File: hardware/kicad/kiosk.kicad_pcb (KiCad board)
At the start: 2 copper layers, 170 x 116 mm, 15 parts, among them J10 TerminalBlock_MaiXu_MX126-5.0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, J11 TerminalBlock_MaiXu_MX126-5.0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, J13 PinHeader_1x09_P2.54mm_Vertic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, J3 PinSocket_1x14_P2.54mm_Vertic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, J4 PinSocket_1x06_P2.54mm_Vertic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, J5 PinSocket_1x04_P2.54mm_Vertic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, J6 PinSocket_1x06_P2.54mm_Vertic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, J7 PinSocket_1x07_P2.54mm_Vertic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, J9 PinHeader_1x03_P2.54mm_Vertic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, U1 ESP32-S3-CAM

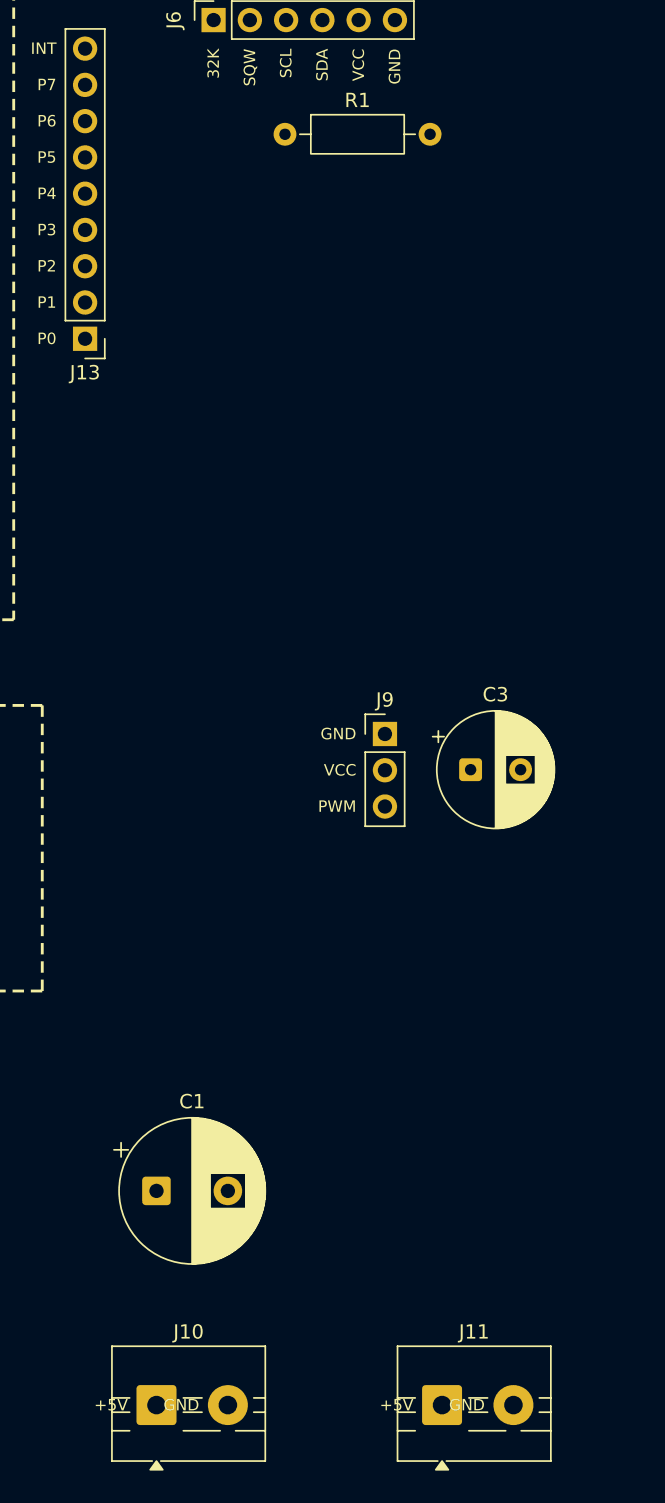
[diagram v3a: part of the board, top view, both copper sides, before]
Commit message: fix(hardware): keep the terminal labels off the neighbouring screw
Both 5 V inputs are two-pad screw terminals at 5.00 mm pitch, and the
label for each pad was set 2 mm inboard of it. On a two-pad row that puts
the text between the pads: "GND" landed on the copper of the +5V screw on
J10 and J11 both. Read off the finished board, either supply would have
gone in backwards. Labels on a two-pad row now grow outward past their own
end, where nothing else can claim them.

R1 is turned round. Its two legs want J6.VCC and J6.SDA, which are the
only pads on the board carrying 3V3 and SDA 2.54 mm apart; drawn the other
way the 3V3 leg reached 9.5 mm and the SDA leg 11.0 mm, against 9.4 and
8.4 now.

Every footprint child arrived without a uuid and pcb upgrade minted a
random one for each, so regenerating the board rewrote about 2000 lines
and buried the real change. They are named from the reference and the node
now, and two runs of the generator produce identical files. This commit
still carries the one-time rewrite.

Task: E14-T8
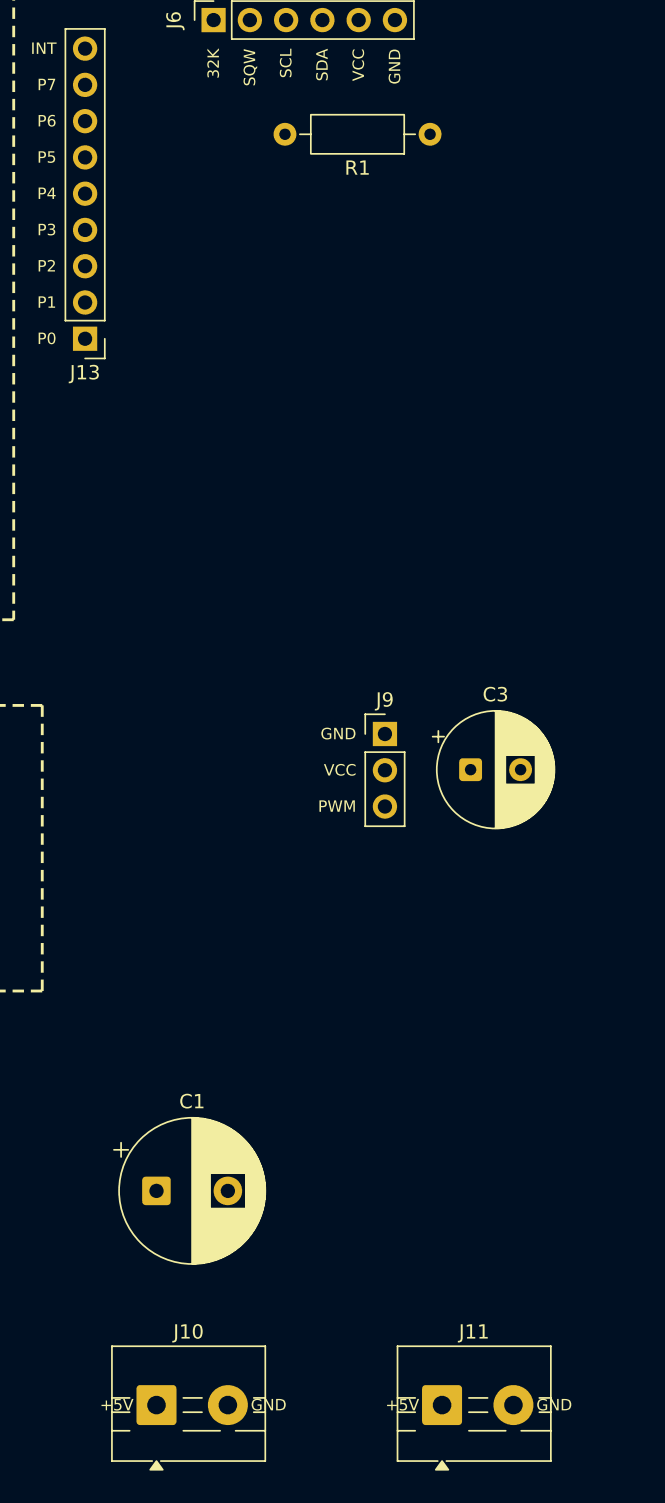
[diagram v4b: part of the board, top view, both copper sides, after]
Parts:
- moved R1 10.2 mm to (153.2, 20.0), turned to 180 degrees
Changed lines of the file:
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@@
 	(footprint "Resistor_THT:R_Axial_DIN0207_L6.3mm_D2.5mm_P10.16mm_Horizontal"
 		(layer "F.Cu")
-		(at 143 20)
+		(at 153.16 20 180)
 		(descr "Resistor, Axial_DIN0207 series, Axial, Horizontal, pin pitch=10.16mm, 0.25W = 1/4W, length*diameter=6.3*2.5mm^2, http://cdn-reichelt.de/documents/datenblatt/B400/1_4W%23YAG.pdf")
 		(tags "Resistor Axial_DIN0207 series Axial Horizontal pin pitch 10.16mm 0.25W = 1/4W length 6.3mm diameter 2.5mm")
 		(property "Reference" "R1"
-			(at 5.08 -2.37 0)
+			(at 5.08 -2.37 180)
 			(layer "F.SilkS")
 			(effects
@@
 		)
 		(property "Value" "R_Axial_DIN0207_L6.3mm_D2.5mm_P10.16mm_Horizontal"
-			(at 5.08 2.37 0)
+			(at 5.08 2.37 180)
 			(layer "F.Fab")
 			(effects
@@
 		)
 		(property "Datasheet" ""
-			(at 0 0 0)
+			(at 0 0 180)
 			(layer "F.Fab")
 			(hide yes)
@@
 		)
 		(property "Description" ""
-			(at 0 0 0)
+			(at 0 0 180)
 			(layer "F.Fab")
 			(hide yes)
@@
 		)
 		(property "KiLib_Generator" "resistor/THT"
-			(at 0 0 0)
+			(at 0 0 180)
 			(layer "F.SilkS")
 			(hide yes)
@@
 		(duplicate_pad_numbers_are_jumpers no)
 		(fp_line
-			(start 1.04 0)
-			(end 1.81 0)
+			(start 9.12 0)
+			(end 8.35 0)
 			(stroke
 				(width 0.12)
@@
 		)
 		(fp_line
-			(start 9.12 0)
-			(end 8.35 0)
+			(start 1.04 0)
+			(end 1.81 0)
 			(stroke
 				(width 0.12)
@@
 		)
 		(fp_line
-			(start 0 0)
-			(end 1.93 0)
+			(start 10.16 0)
+			(end 8.23 0)
 			(stroke
 				(width 0.1)
@@
 		)
 		(fp_line
-			(start 10.16 0)
-			(end 8.23 0)
+			(start 0 0)
+			(end 1.93 0)
 			(stroke
 				(width 0.1)
@@
 		)
 	)
+	(gr_text "GND"
+		(at 140.6 109 0)
+		(layer "F.SilkS")
+		(effects
+			(font
+				(size 0.8 0.8)
+				(thickness 0.12)
+			)
+			(justify left)
+		)
+	)
+	(gr_text "GND"
+		(at 160.6 109 0)
+		(layer "F.SilkS")
+		(effects
+			(font
+				(size 0.8 0.8)
+				(thickness 0.12)
+			)
+			(justify left)
+		)
+	)
 	(gr_text "IO43"
 		(at 28.7 37.87 0)
@@
 	)
 	(gr_text "+5V"
-		(at 132 109 0)
-		(layer "F.SilkS")
-		(effects
-			(font
-				(size 0.8 0.8)
-				(thickness 0.12)
-			)
-			(justify right)
-		)
-	)
-	(gr_text "GND"
-		(at 137 109 0)
+		(at 132.4 109 0)
 		(layer "F.SilkS")
 		(effects
@@
 	)
 	(gr_text "+5V"
-		(at 152 109 0)
-		(layer "F.SilkS")
-		(effects
-			(font
-				(size 0.8 0.8)
-				(thickness 0.12)
-			)
-			(justify right)
-		)
-	)
-	(gr_text "GND"
-		(at 157 109 0)
+		(at 152.4 109 0)
 		(layer "F.SilkS")
 		(effects

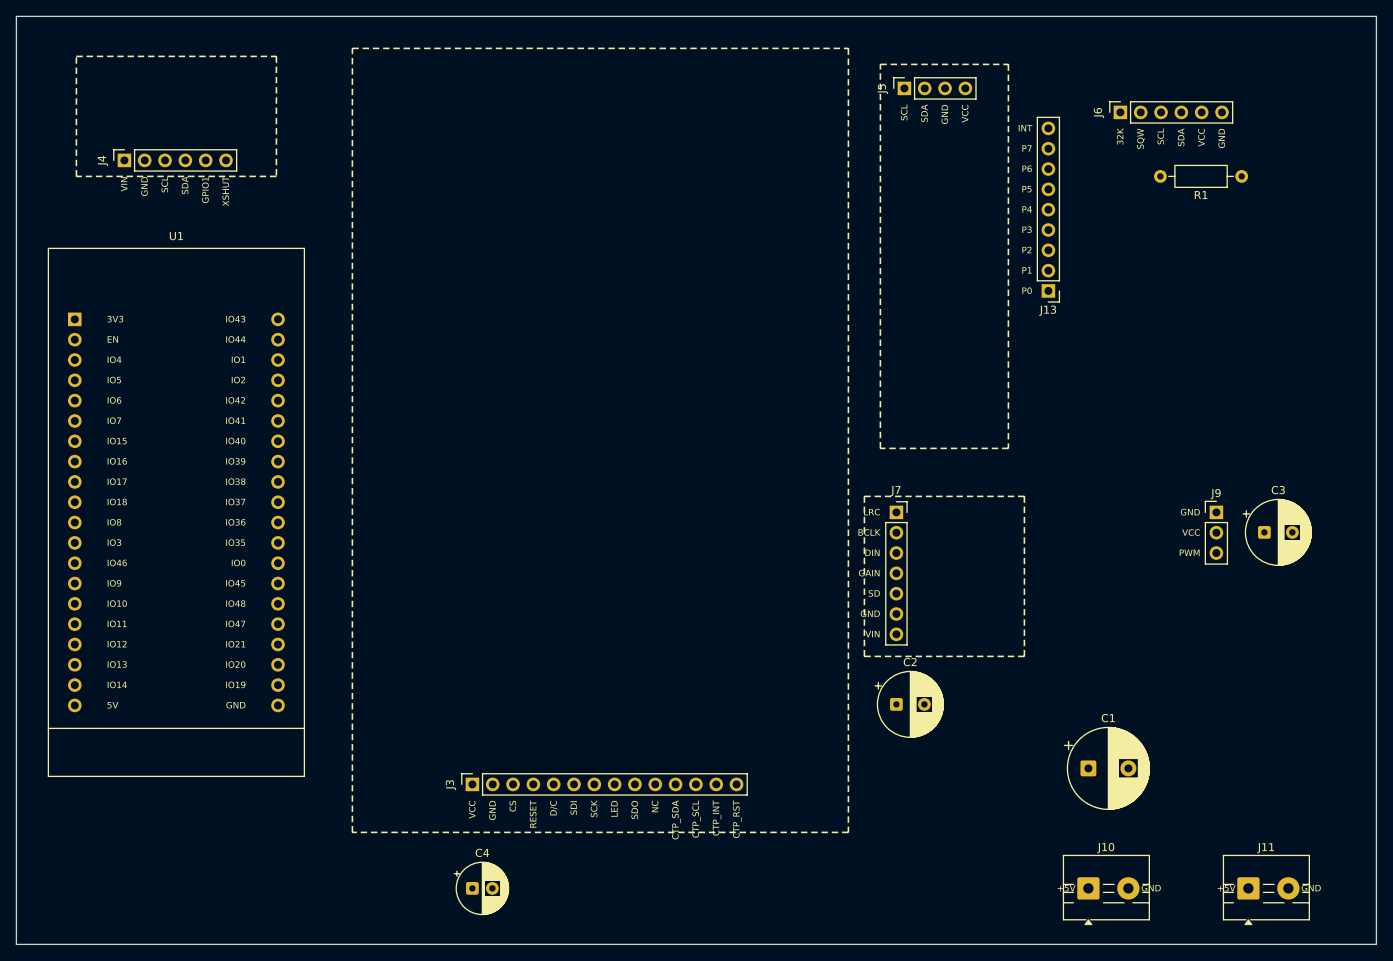
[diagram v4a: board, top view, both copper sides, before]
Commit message: feat(hardware): bolt the panel down and cut the board to the parts
The panel plugs into J3 along one edge and the opposite edge was free. A
kiosk stands the panel upright, so its weight and every touch press went
into fourteen solder joints, which take compression well and leverage
badly: they crack as hairlines, drop one pin intermittently, and read
exactly like a firmware fault. Four M2.5 holes at the panel's corners now
carry it on 8.5 mm standoffs, the same height the socket holds it at, so
the header carries signal and nothing else.

The panel measures 107 x 61, not the 62 x 98 that was estimated. It is
nine millimetres longer than the board had room for, which leaves no strip
underneath it at all, so C4 moves to the left of the panel below the
devkit. The two numbers that place the holes are still unmeasured and are
named at the top of gen_pcb.py; the panel rectangle is now derived from
J3 rather than written out, so correcting them moves everything at once.

R1 and C3 are centred on J6 and J9. The rail-2 column moves 7 mm inward
keeping J11's offset from J9, so rule 2 of section 2.5 is unchanged, and
the board goes from 170 to 158 wide.

check_pcb gains two things it was blind to: courtyards drawn as circles,
which is every capacitor and every mounting hole, and a rule that one
module body holds one part's pins. Proven by moving C2 inside the
amplifier's outline and watching it fail.

Task: E14-T8
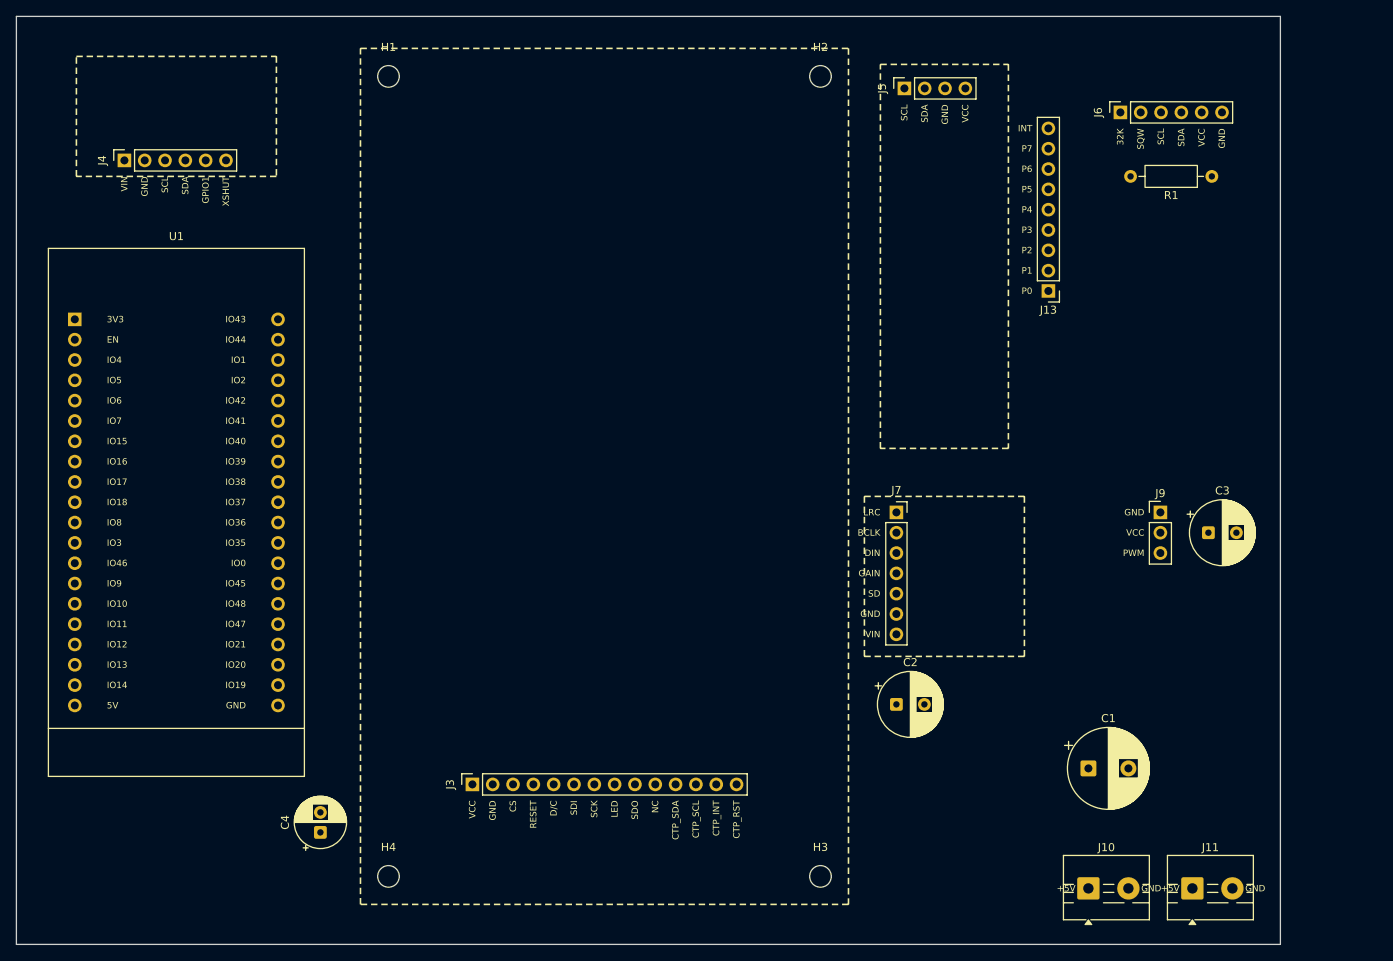
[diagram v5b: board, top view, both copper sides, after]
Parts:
- added H1: MountingHole_2.7mm, MountingHole:MountingHole_2.7mm, F.Cu at (46.5, 7.50)
- added H2: MountingHole_2.7mm, MountingHole:MountingHole_2.7mm, F.Cu at (100.5, 7.50)
- added H3: MountingHole_2.7mm, MountingHole:MountingHole_2.7mm, F.Cu at (100.5, 107.5)
- added H4: MountingHole_2.7mm, MountingHole:MountingHole_2.7mm, F.Cu at (46.5, 107.5)
- moved C4 20.2 mm to (38.0, 102.0), turned to 90 degrees
- moved C3 7.00 mm to (149.0, 64.5)
- moved J11 7.00 mm to (147.0, 109.0)
- moved J9 7.00 mm to (143.0, 62.0)
- moved R1 3.73 mm to (149.4, 20.0)
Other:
- board size 170 x 116 mm -> 158 x 116 mm

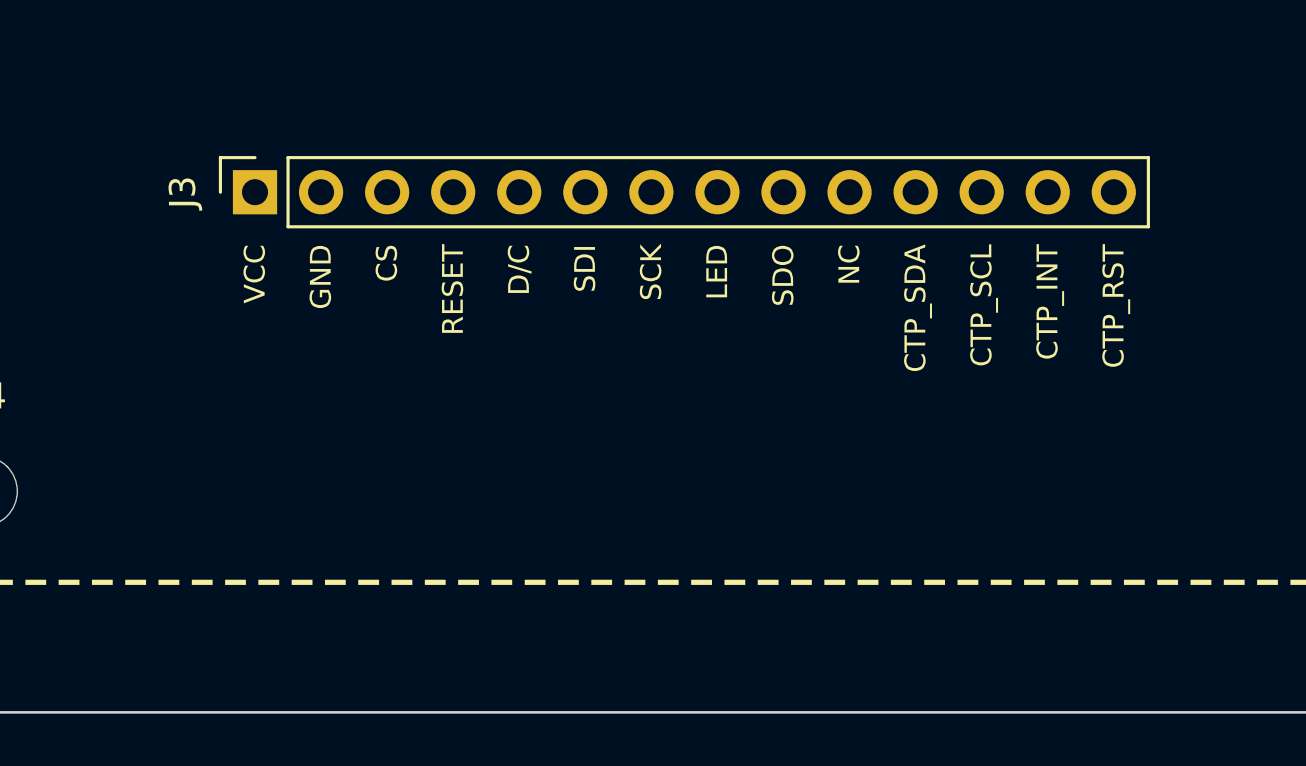
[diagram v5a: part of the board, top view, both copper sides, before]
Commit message: fix(hardware): seat the panel's header in the strip past the glass
A 4.0 inch 3:2 panel shows 84.5 x 56.4 mm, so a 107 x 61 PCB leaves
11.2 mm past each short edge and only 2.3 mm past each long one. That
kills two guesses at once.

LCD_HEADER_INSET was 15 mm, which would put the fourteen-pin row under
the glass. It cannot exceed 11.2, and a row centred in that strip lands
near 6, so it is 6 now. Holding J3 still and shrinking the inset would
have pushed the panel five millimetres off the top edge of the board, so
J3 drops the same nine millimetres it lost: the panel rectangle and all
four holes stay exactly where they were, and only the socket moves.

The 2.3 mm along the long edges is why the holes belong at the corners
rather than halfway down the sides: a 2.7 mm hole does not fit in 2.3 mm
of material, and the corners are the only place with any.

Task: E14-T8
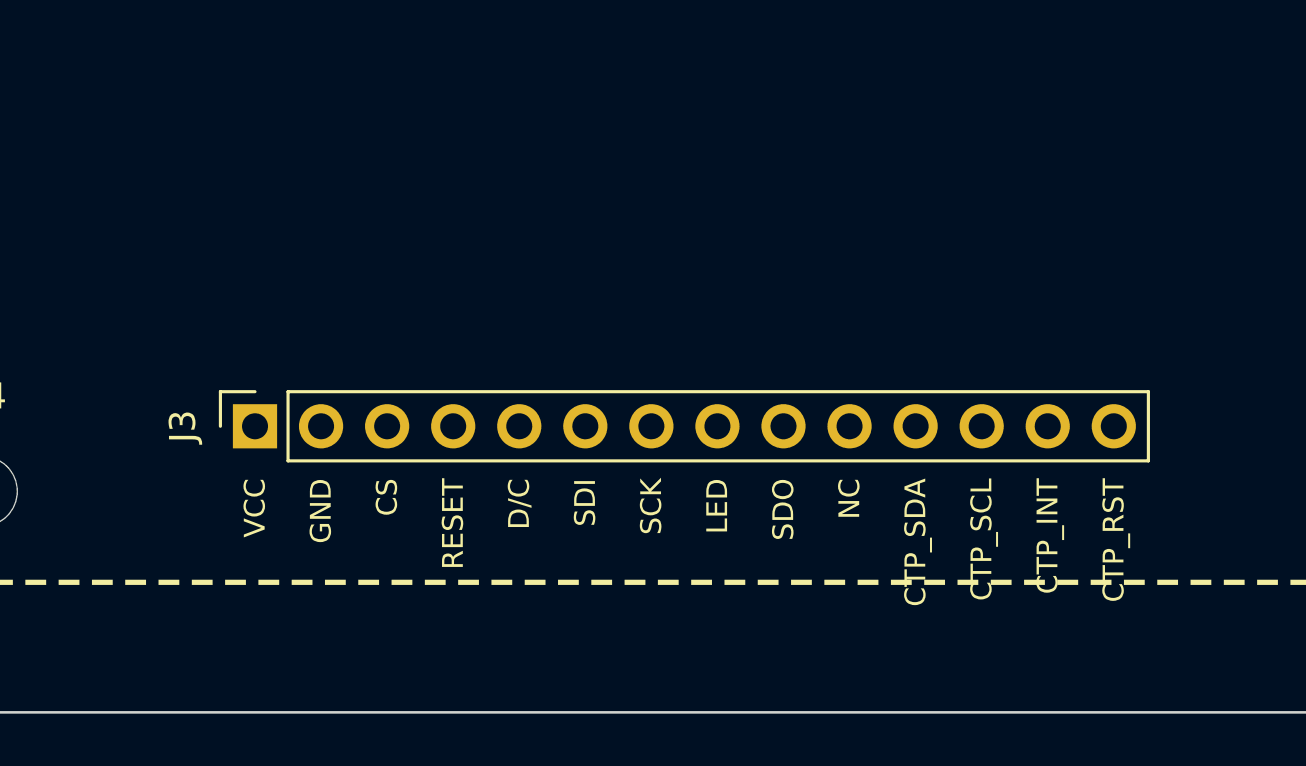
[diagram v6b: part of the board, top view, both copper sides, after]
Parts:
- moved J3 9.00 mm to (57.0, 105.0)
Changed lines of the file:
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@@
 	(footprint "Connector_PinSocket_2.54mm:PinSocket_1x14_P2.54mm_Vertical"
 		(layer "F.Cu")
-		(at 57 96 90)
+		(at 57 105 90)
 		(descr "Through hole straight socket strip, 1x14, 2.54mm pitch, single row (from Kicad 4.0.7), script generated")
 		(tags "Through hole socket strip THT 1x14 2.54mm single row")
@@
 	)
 	(gr_text "VCC"
-		(at 57 98 90)
+		(at 57 107 90)
 		(layer "F.SilkS")
 		(effects
@@
 	)
 	(gr_text "GND"
-		(at 59.54 98 90)
+		(at 59.54 107 90)
 		(layer "F.SilkS")
 		(effects
@@
 	)
 	(gr_text "CS"
-		(at 62.08 98 90)
+		(at 62.08 107 90)
 		(layer "F.SilkS")
 		(effects
@@
 	)
 	(gr_text "RESET"
-		(at 64.62 98 90)
+		(at 64.62 107 90)
 		(layer "F.SilkS")
 		(effects
@@
 	)
 	(gr_text "D/C"
-		(at 67.16 98 90)
+		(at 67.16 107 90)
 		(layer "F.SilkS")
 		(effects
@@
 	)
 	(gr_text "SDI"
-		(at 69.7 98 90)
+		(at 69.7 107 90)
 		(layer "F.SilkS")
 		(effects
@@
 	)
 	(gr_text "SCK"
-		(at 72.24 98 90)
+		(at 72.24 107 90)
 		(layer "F.SilkS")
 		(effects
@@
 	)
 	(gr_text "LED"
-		(at 74.78 98 90)
+		(at 74.78 107 90)
 		(layer "F.SilkS")
 		(effects
@@
 	)
 	(gr_text "SDO"
-		(at 77.32 98 90)
+		(at 77.32 107 90)
 		(layer "F.SilkS")
 		(effects
@@
 	)
 	(gr_text "NC"
-		(at 79.86 98 90)
+		(at 79.86 107 90)
 		(layer "F.SilkS")
 		(effects
@@
 	)
 	(gr_text "CTP_SDA"
-		(at 82.4 98 90)
+		(at 82.4 107 90)
 		(layer "F.SilkS")
 		(effects
@@
 	)
 	(gr_text "CTP_SCL"
-		(at 84.94 98 90)
+		(at 84.94 107 90)
 		(layer "F.SilkS")
 		(effects
@@
 	)
 	(gr_text "CTP_INT"
-		(at 87.48 98 90)
+		(at 87.48 107 90)
 		(layer "F.SilkS")
 		(effects
@@
 	)
 	(gr_text "CTP_RST"
-		(at 90.02 98 90)
+		(at 90.02 107 90)
 		(layer "F.SilkS")
 		(effects
